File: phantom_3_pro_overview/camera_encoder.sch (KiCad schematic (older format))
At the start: 0 parts

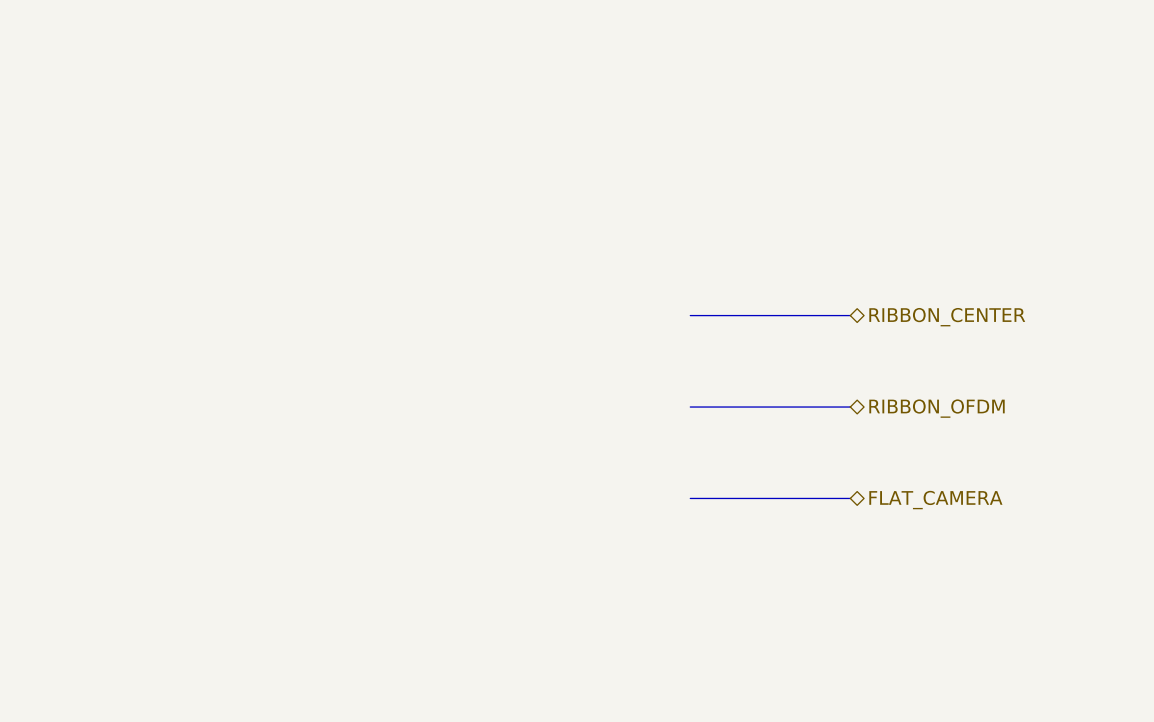
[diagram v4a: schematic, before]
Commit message: Overview: Drawn the camera encoder block.
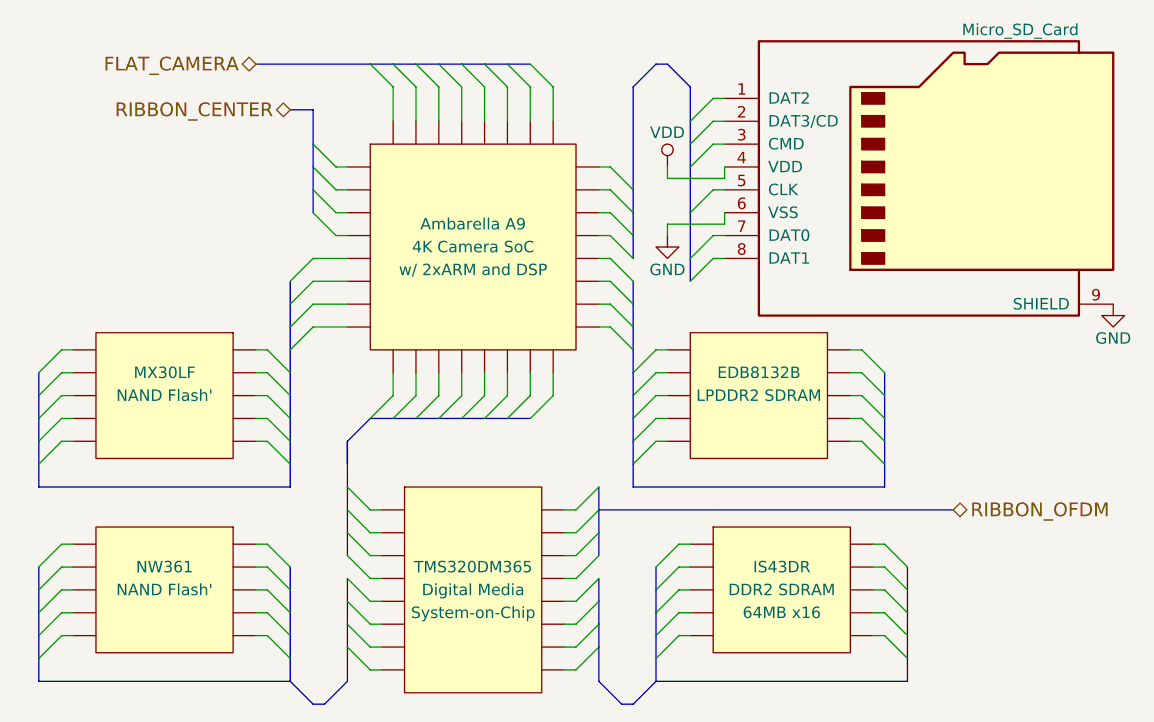
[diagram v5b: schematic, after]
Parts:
- added J?: Micro_SD_Card, symbol Micro_SD_Card
- added U?: Ambarella A9, 4K Camera SoC, symbol IC_PQFP32
- added U?: TMS320DM365, Digital Media, symbol IC_DIL16
- added U?: IS43DR, DDR2 SDRAM, symbol IC_DIL10
- added U?: NW361, NAND Flash', symbol IC_DIL10
- added U?: EDB8132B, LPDDR2 SDRAM, symbol IC_DIL10
- added U?: MX30LF, NAND Flash', symbol IC_DIL10
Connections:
- new net GND: J?.6 (VSS), J?.9 (SHIELD)
- new net VDD: J?.4 (VDD)

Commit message: Overview: Started work on camera sensor brd.
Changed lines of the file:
@@
 LIBS:transistors-switches
 LIBS:transistors-power
+LIBS:sensors-v2
+LIBS:regul-v2
 LIBS:phantom_3_pro_overview-cache
 EELAYER 25 0
@@
 	1750 1850 1900 1850
 Wire Bus Line
-	3400 800  3400 950
-Wire Bus Line
-	3400 950  3400 1050
-Wire Bus Line
-	3400 1050 3400 1150
-Wire Bus Line
-	3400 1150 3400 1350
-Wire Bus Line
-	3400 1350 3400 1550
-Wire Bus Line
-	3400 1550 3400 1650
-Wire Bus Line
-	1500 700  2000 700
-Wire Bus Line
-	2000 700  2100 700
-Wire Bus Line
-	2100 700  2200 700
-Wire Bus Line
-	2200 700  2300 700
-Wire Bus Line
-	2300 700  2400 700
-Wire Bus Line
-	2400 700  2500 700
-Wire Bus Line
-	2500 700  2600 700
-Wire Bus Line
-	2600 700  2700 700
+	3400 800  3400 1650
+Wire Bus Line
+	1500 700  2700 700
 Wire Bus Line
 	3250 700  3300 700
@@
 	2000 2650 1900 2550
 Wire Bus Line
-	1900 2350 1900 2450
-Wire Bus Line
-	1900 2350 1900 2550
-Wire Bus Line
-	1900 2550 1900 2650
-Wire Bus Line
-	1900 2650 1900 2750
-Wire Bus Line
-	1900 2750 1900 2850
+	1900 2350 1900 2850
 Entry Wire Line
 	2900 3350 3000 3250
@@
 	2900 2650 3000 2550
 Wire Bus Line
-	1750 900  1750 1050
-Wire Bus Line
-	1750 1050 1750 1150
-Wire Bus Line
-	1750 1150 1750 1250
-Wire Bus Line
-	1750 1250 1750 1350
+	1750 900  1750 1350
 Wire Wire Line
 	2000 2650 2050 2650
@@
 	3150 3500 3250 3400
 Wire Bus Line
-	3250 2900 3250 3000
-Wire Bus Line
-	3250 3000 3250 3100
-Wire Bus Line
-	3250 3100 3250 3200
-Wire Bus Line
-	3250 3200 3250 3300
-Wire Bus Line
-	3250 3300 3250 3400
+	3250 2900 3250 3400
 Wire Bus Line
 	3100 3500 3150 3500
@@
 	3400 3200 3350 3200
 Wire Bus Line
-	4350 2900 4350 3000
-Wire Bus Line
-	4350 3000 4350 3100
-Wire Bus Line
-	4350 3100 4350 3200
-Wire Bus Line
-	4350 3200 4350 3300
-Wire Bus Line
-	4350 3300 4350 3400
+	4350 2900 4350 3400
 Wire Bus Line
 	4350 3400 3250 3400
 Wire Bus Line
-	3000 2550 3000 2650
-Wire Bus Line
-	3000 2650 3000 2750
-Wire Bus Line
-	3000 2750 3000 2850
-Wire Bus Line
-	3000 2950 3000 3050
-Wire Bus Line
-	3000 3050 3000 3150
-Wire Bus Line
-	3000 3150 3000 3250
-Wire Bus Line
-	3000 3250 3000 3400
+	3000 2550 3000 2850
+Wire Bus Line
+	3000 2950 3000 3400
 $Comp
 L IC_DIL10 U?
@@
 	1750 3500 1650 3400
 Wire Bus Line
-	1650 2900 1650 3000
-Wire Bus Line
-	1650 3000 1650 3100
-Wire Bus Line
-	1650 3100 1650 3200
-Wire Bus Line
-	1650 3200 1650 3300
-Wire Bus Line
-	1650 3300 1650 3400
+	1650 2900 1650 3400
 Wire Bus Line
 	1800 3500 1750 3500
@@
 	1500 3200 1550 3200
 Wire Bus Line
-	550  2900 550  3000
-Wire Bus Line
-	550  3000 550  3100
-Wire Bus Line
-	550  3100 550  3200
-Wire Bus Line
-	550  3200 550  3300
-Wire Bus Line
-	550  3300 550  3400
+	550  2900 550  3400
 Wire Bus Line
 	550  3400 1650 3400
 Wire Bus Line
-	1900 2950 1900 3050
-Wire Bus Line
-	1900 3050 1900 3150
-Wire Bus Line
-	1900 3150 1900 3250
-Wire Bus Line
-	1900 3250 1900 3400
+	1900 2950 1900 3400
 $Comp
 L IC_DIL10 U?
@@
 $EndComp
 Wire Bus Line
-	3150 1650 3150 1750
-Wire Bus Line
-	3150 1750 3150 1850
-Wire Bus Line
-	3150 1850 3150 1950
-Wire Bus Line
-	3150 1950 3150 2050
-Wire Bus Line
-	3150 2050 3150 2150
-Wire Bus Line
-	3150 2150 3150 2250
-Wire Bus Line
-	3150 2250 3150 2350
-Wire Bus Line
-	3150 2350 3150 2450
-Wire Bus Line
-	3150 2450 3150 2550
+	3150 1650 3150 2550
 Entry Wire Line
 	4250 2450 4150 2350
@@
 	3300 2350 3250 2350
 Wire Bus Line
-	4250 2050 4250 2150
-Wire Bus Line
-	4250 2150 4250 2250
-Wire Bus Line
-	4250 2250 4250 2350
-Wire Bus Line
-	4250 2350 4250 2450
-Wire Bus Line
-	4250 2450 4250 2550
+	4250 2050 4250 2550
 Wire Bus Line
 	4250 2550 3150 2550
 Wire Bus Line
-	3150 800  3150 800
-Wire Bus Line
-	3150 800  3150 1250
-Wire Bus Line
-	3150 1250 3150 1350
-Wire Bus Line
-	3150 1350 3150 1450
-Wire Bus Line
-	3150 1450 3150 1550
+	3150 800  3150 1550
 Wire Bus Line
 	3000 2650 4550 2650
@@
 $EndComp
 Wire Bus Line
-	1650 1650 1650 1750
-Wire Bus Line
-	1650 1750 1650 1850
-Wire Bus Line
-	1650 1850 1650 1950
-Wire Bus Line
-	1650 1950 1650 2050
-Wire Bus Line
-	1650 2050 1650 2150
-Wire Bus Line
-	1650 2150 1650 2250
-Wire Bus Line
-	1650 2250 1650 2350
-Wire Bus Line
-	1650 2350 1650 2450
-Wire Bus Line
-	1650 2450 1650 2550
+	1650 1650 1650 2550
 Entry Wire Line
 	550  2450 650  2350
@@
 	1500 2350 1550 2350
 Wire Bus Line
-	550  2050 550  2150
-Wire Bus Line
-	550  2150 550  2250
-Wire Bus Line
-	550  2250 550  2350
-Wire Bus Line
-	550  2350 550  2450
-Wire Bus Line
-	550  2450 550  2550
+	550  2050 550  2550
 Wire Bus Line
 	550  2550 1650 2550
 Wire Bus Line
-	2000 2250 2100 2250
-Wire Bus Line
-	2100 2250 2200 2250
-Wire Bus Line
-	2200 2250 2300 2250
-Wire Bus Line
-	2300 2250 2400 2250
-Wire Bus Line
-	2400 2250 2500 2250
-Wire Bus Line
-	2500 2250 2600 2250
-Wire Bus Line
-	2600 2250 2700 2250
+	2000 2250 2700 2250
 Entry Bus Bus
 	1900 2350 2000 2250

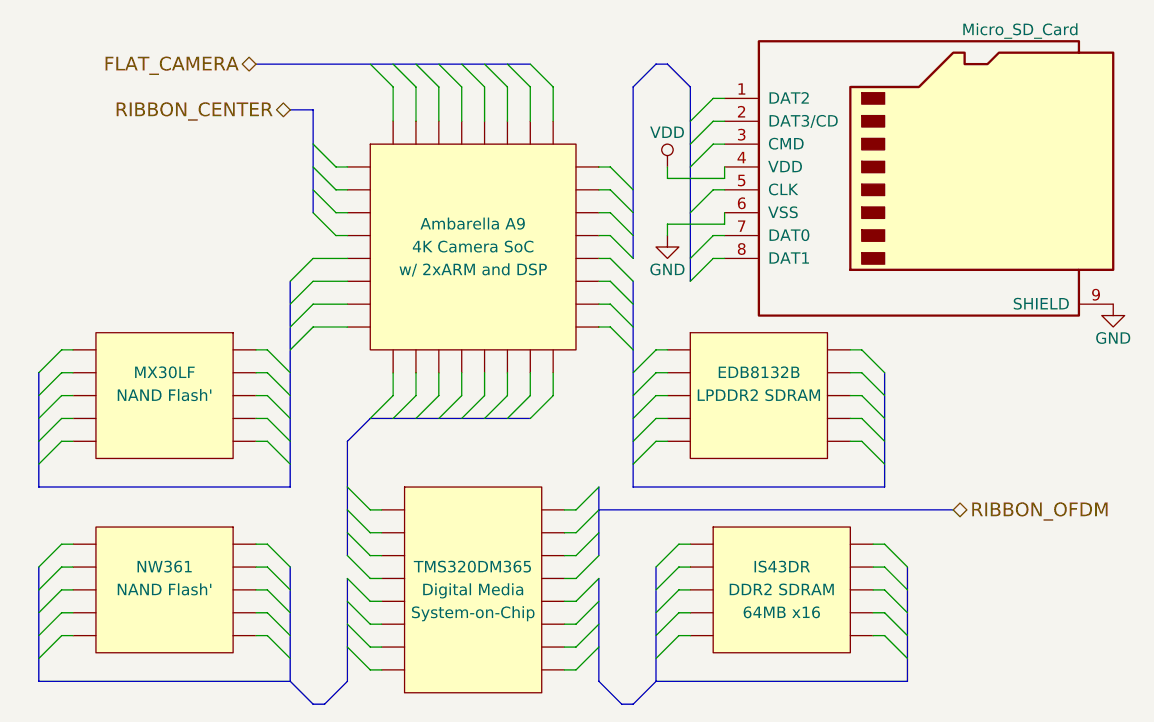
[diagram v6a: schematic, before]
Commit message: Overview: Updated to latest findings.
Added magnetometer to gimbal control, and made some minor fixes.
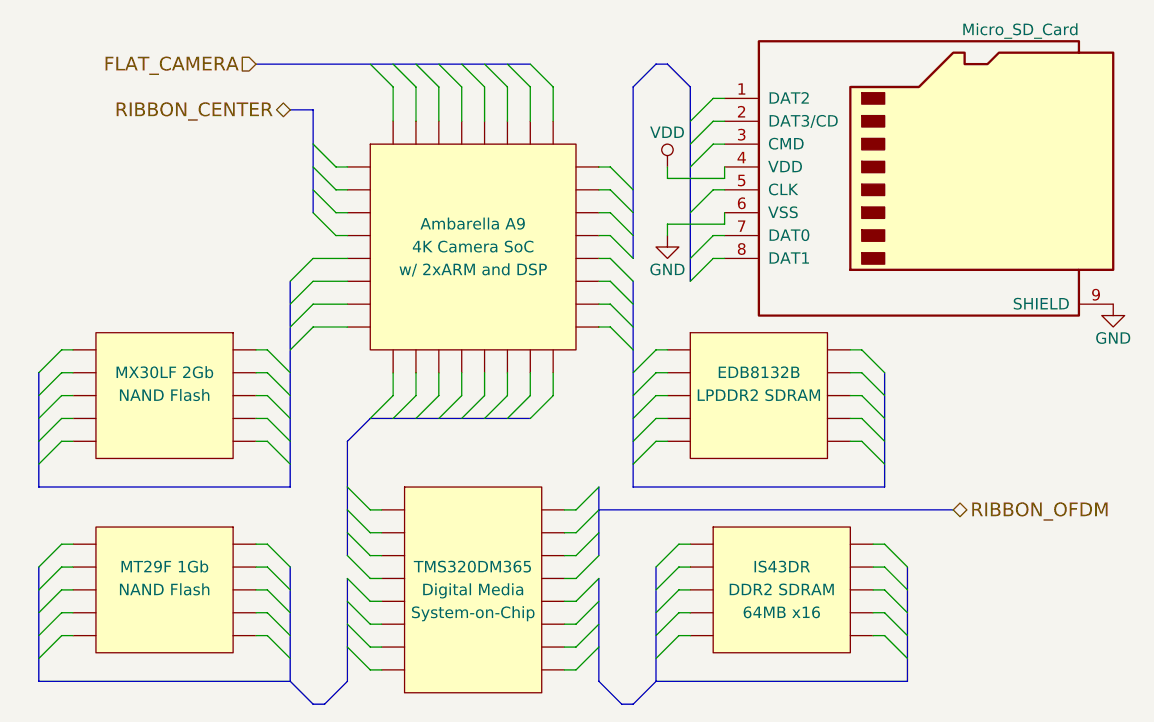
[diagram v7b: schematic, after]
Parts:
- U?: value NW361 -> MT29F 1Gb; footprint NAND Flash' -> NAND Flash
- U?: value MX30LF -> MX30LF 2Gb; footprint NAND Flash' -> NAND Flash
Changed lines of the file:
@@
 Text HLabel 4550 2650 2    60   BiDi ~ 0
 RIBBON_OFDM
-Text HLabel 1500 700  0    60   BiDi ~ 0
+Text HLabel 1500 700  0    60   Input ~ 0
 FLAT_CAMERA
 $Comp
@@
 P 1100 3000
 F 0 "U?" H 1100 2900 50  0001 C CNN
-F 1 "NW361" H 1100 3100 50  0000 C CNN
-F 2 "NAND Flash'" H 1100 3000 50  0000 C CNN
+F 1 "MT29F 1Gb" H 1100 3100 50  0000 C CNN
+F 2 "NAND Flash" H 1100 3000 50  0000 C CNN
 F 3 "DOCUMENTATION" H 1100 3000 50  0001 C CNN
 	1    1100 3000
@@
 P 1100 2150
 F 0 "U?" H 1100 2050 50  0001 C CNN
-F 1 "MX30LF" H 1100 2250 50  0000 C CNN
-F 2 "NAND Flash'" H 1100 2150 50  0000 C CNN
+F 1 "MX30LF 2Gb" H 1100 2250 50  0000 C CNN
+F 2 "NAND Flash" H 1100 2150 50  0000 C CNN
 F 3 "DOCUMENTATION" H 1100 2150 50  0001 C CNN
 	1    1100 2150

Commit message: Overview: Separated gimbal power circuit.
This is to make sure the connection won't be interpreted as data link.
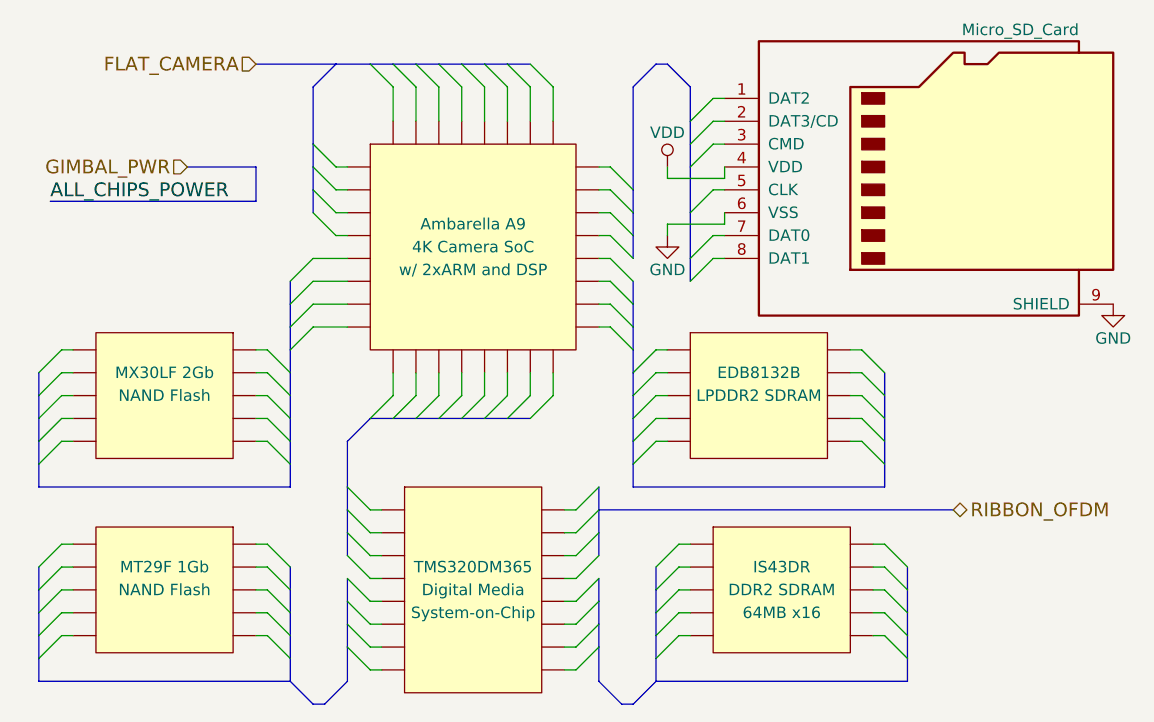
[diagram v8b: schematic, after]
